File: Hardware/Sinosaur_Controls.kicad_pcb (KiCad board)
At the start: 2 copper layers, 70.8 x 110 mm, 30 parts, among them J1 Conn_01x12_Pin, J10 Audio_Out_L, J11 Audio_Out_R, J12 USB_C_Receptacle, J14 Conn_01x01_Socket, J2 Conn_01x12_Pin, J3 Conn_01x10_Pin, J4 Conn_01x10_Pin, J5 WavetablePosA, J6 WavetablePosB, J7 WarpCV, J8 VOct, J9 VCA, SW1 B_Octave, SW2 Mode_Switch, SW3 Octave_Switch, SW4 ChB_Output, SW5 Encoder, U1 STF202-22T1G

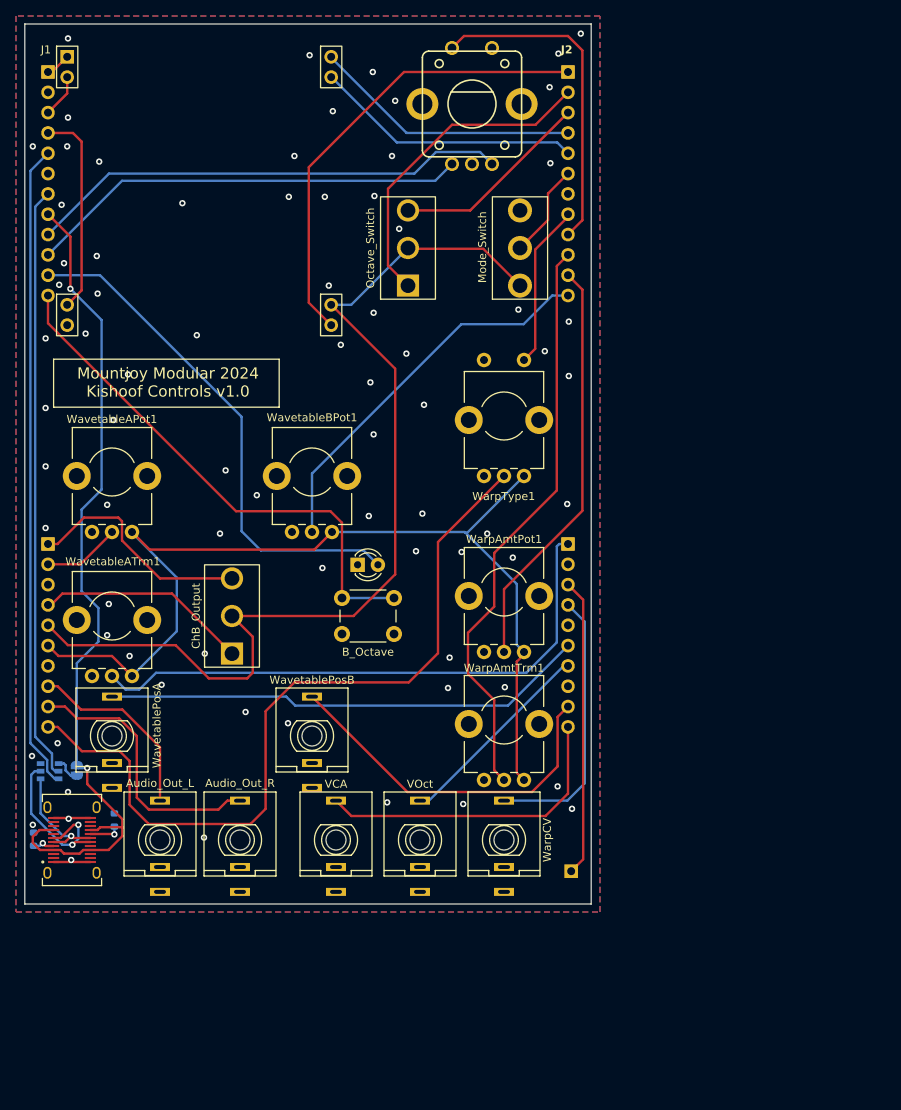
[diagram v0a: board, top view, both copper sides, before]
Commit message: Started control layout
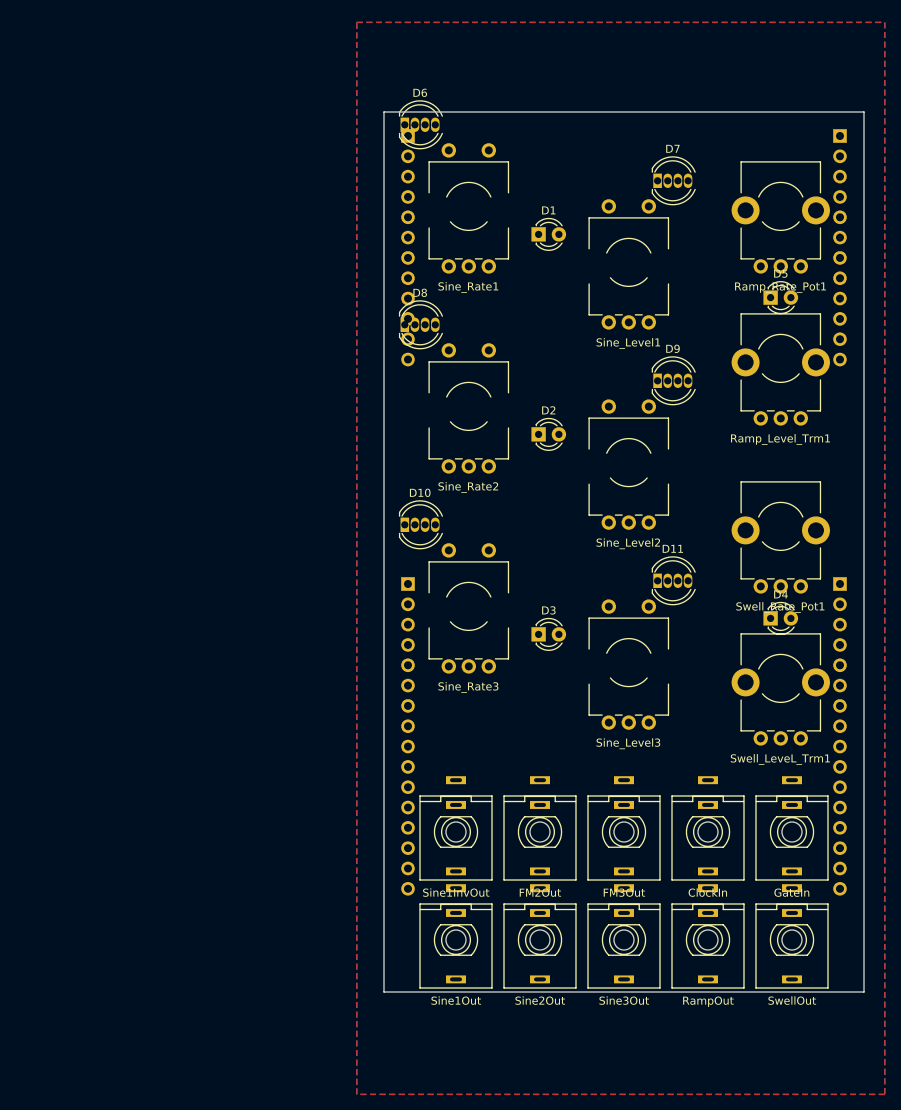
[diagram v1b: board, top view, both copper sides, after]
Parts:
- removed JP1: Jumper, Jumper:SolderJumper-2_P1.3mm_Open_RoundedPad1.0x1.5mm
- removed R1, R2: 5k1, Resistor_SMD:R_0603_1608Metric
- removed SW1: B_Octave, Custom_Footprints:SW_PUSH_6mm_aligned
- removed SW2: Mode_Switch, Custom_Footprints:SPDT_Miniature
- removed SW3: Octave_Switch, Custom_Footprints:SP3T_Mini_Switch
- removed SW4: ChB_Output, Custom_Footprints:SP3T_Mini_Switch
- removed SW5: Encoder, Custom_Footprints:Encoder
- removed U1: STF202-22T1G, Custom_Footprints:STF202-22T1G
- removed U2: ~, Custom_Footprints:LCD_Riser
- removed WarpAmtPot1, WarpAmtTrm1, WavetableAPot1, WavetableATrm1, WavetableBPot1: B10k, Custom_Footprints:Alpha_9mm_Potentiometer_Aligned
- removed WarpType1: WarpTypePot, Custom_Footprints:Bourns_Switch_Potentiometer
- added D10: LED_BGAR, LED_THT:LED_D5.0mm-4_RGB, F.Cu at (102.6, 101.6)
- added D11: LED_BGAR, LED_THT:LED_D5.0mm-4_RGB, F.Cu at (134.2, 108.6)
- added D2: LED, LED_THT:LED_D3.0mm_FlatTop, F.Cu at (119.3, 90.3)
- added D3: LED, LED_THT:LED_D3.0mm_FlatTop, F.Cu at (119.3, 115.3)
- added D4: LED, LED_THT:LED_D3.0mm_FlatTop, F.Cu at (148.3, 113.3)
- added D5: LED, LED_THT:LED_D3.0mm_FlatTop, F.Cu at (148.3, 73.2)
- added D6: LED_BGAR, LED_THT:LED_D5.0mm-4_RGB, F.Cu at (102.6, 51.6)
- added D7: LED_BGAR, LED_THT:LED_D5.0mm-4_RGB, F.Cu at (134.2, 58.6)
- added D8: LED_BGAR, LED_THT:LED_D5.0mm-4_RGB, F.Cu at (102.6, 76.6)
- added D9: LED_BGAR, LED_THT:LED_D5.0mm-4_RGB, F.Cu at (134.2, 83.6)
- added J13: SwellOut, Custom_Footprints:THONKICONN_hole, F.Cu at (151.0, 153.5)
- added Ramp_Level_Trm1: B10k, Custom_Footprints:Alpha_9mm_Potentiometer_Aligned, F.Cu at (149.6, 80.8)
- added Ramp_Rate_Pot1: B10k, Custom_Footprints:Alpha_9mm_Potentiometer_Aligned, F.Cu at (149.6, 61.8)
- added Sine_Level1: Switch_10kPot, Custom_Footprints:Bourns_Switch_Potentiometer, F.Cu at (130.6, 68.8)
- added Sine_Level2: Switch_10kPot, Custom_Footprints:Bourns_Switch_Potentiometer, F.Cu at (130.6, 93.8)
- added Sine_Level3: Switch_10kPot, Custom_Footprints:Bourns_Switch_Potentiometer, F.Cu at (130.6, 118.8)
- added Sine_Rate1: Switch_10kPot, Custom_Footprints:Bourns_Switch_Potentiometer, F.Cu at (110.6, 61.8)
- added Sine_Rate2: Switch_10kPot, Custom_Footprints:Bourns_Switch_Potentiometer, F.Cu at (110.6, 86.8)
- added Sine_Rate3: Switch_10kPot, Custom_Footprints:Bourns_Switch_Potentiometer, F.Cu at (110.6, 111.8)
- added Swell_LeveL_Trm1: B10k, Custom_Footprints:Alpha_9mm_Potentiometer_Aligned, F.Cu at (149.6, 120.8)
- added Swell_Rate_Pot1: B10k, Custom_Footprints:Alpha_9mm_Potentiometer_Aligned, F.Cu at (149.6, 101.8)
- D1: value LED_Small -> LED
- J1: value Conn_01x12_Pin -> Conn_01x12_Male
- J10: value Audio_Out_L -> Sine1InvOut
- J11: value Audio_Out_R -> FM2Out
- J12: value USB_C_Receptacle -> FM3Out; footprint Custom_Footprints:USB_C_Receptacle_Amphenol_12401951E412A -> Custom_Footprints:THONKICONN_hole
- J14: value Conn_01x01_Socket -> ClockIn; footprint Connector_PinHeader_2.54mm:PinHeader_1x01_P2.54mm_Vertical -> Custom_Footprints:THONKICONN_hole; moved to F.Cu
- J2: value Conn_01x12_Pin -> Conn_01x16_Male; footprint Connector_PinSocket_2.54mm:PinSocket_1x12_P2.54mm_Vertical -> Connector_PinSocket_2.54mm:PinSocket_1x16_P2.54mm_Vertical
- J3: value Conn_01x10_Pin -> Conn_01x12_Male; footprint Connector_PinSocket_2.54mm:PinSocket_1x10_P2.54mm_Vertical -> Connector_PinSocket_2.54mm:PinSocket_1x12_P2.54mm_Vertical
- J4: value Conn_01x10_Pin -> Conn_01x16_Male; footprint Connector_PinSocket_2.54mm:PinSocket_1x10_P2.54mm_Vertical -> Connector_PinSocket_2.54mm:PinSocket_1x16_P2.54mm_Vertical
- J5: value WavetablePosA -> Sine1Out
- J6: value WavetablePosB -> Sine2Out
- J7: value WarpCV -> Sine3Out
- J8: value VOct -> RampOut
- J9: value VCA -> GateIn
- moved J1 99.3 mm to (157.0, 53.0)
- moved J2 72.5 mm to (157.0, 109.0)
- moved J12 69.0 mm to (130.0, 140.0), turned to 180 degrees
- moved J3 68.0 mm to (103.0, 53.0)
- moved J9 57.0 mm to (151.0, 140.0), turned to 180 degrees
- moved J5 50.0 mm to (109.0, 153.5), turned to 180 degrees
- moved D1 47.1 mm to (119.3, 65.3)
- moved J6 38.2 mm to (119.5, 153.5), turned to 180 degrees
- moved J8 38.1 mm to (140.5, 153.5), turned to 180 degrees
- moved J11 37.5 mm to (119.5, 140.0), turned to 180 degrees
- moved J10 37.0 mm to (109.0, 140.0), turned to 180 degrees
- moved J4 20.6 mm to (103.0, 109.0)
- moved J7 19.5 mm to (130.0, 153.5), turned to 180 degrees
- moved J14 17.8 mm to (140.5, 140.0)
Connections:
- net /Audio_Out_L renamed /Sine1_Inv_Out
- D1 pad 2: /LED_Oct_B_Out -> /Sine1_LED
- J1 pad 1: /LCD_SPI3_MOSI -> GND
- J1 pad 10: /Encoder_Up -> GND
- J1 pad 11: /LED_Oct_B_Out -> /Ramp_Level
- J1 pad 12: /B_Octave_Btn -> /Sine2_Swell_Rate_LED
- J1 pad 2: GND -> /FM3_Out
- J1 pad 3: /LCD_SPI3_SCK -> /FM2_Out
- J1 pad 4: /LCD_SPI3_SS -> /Ramp_Out
- J1 pad 5: /USB_DP -> /Swell_Out
- J1 pad 6: GND -> /Sine1_Level
- J1 pad 7: /USB_DM -> /Sine2_Level
- J1 pad 8: /USB_VBUS -> /Sine3_Rate
- J1 pad 9: /Encoder_Down -> /Ramp_Rate
- J11 pad 3: /Audio_Out_R -> /FM2_Out
- J14 pad 1: /Ext_Audio_In -> GND
- J2 pad 1: /LCD_Backlight -> /Sine1_Swell_Rate_LED
- J2 pad 10: /Warp_Amt_Trm -> /Sine3_Swell_Lvl_LED
- J2 pad 11: /Warp_Amt_Pot -> /Sine1_Ramp_Rate_LED
- J2 pad 12: /Wavetable_Pos_B_Pot -> /Sine2_Rate
- J2 pad 2: /Octave_Up -> /Swell_Rate
- J2 pad 3: /Octave_Down -> /Sine3_Ramp_Rate_LED
- J2 pad 4: /LCD_DC -> /Sine1_Ramp_Lvl_LED
- J2 pad 5: /LCD_RESET -> /Sine2_Ramp_Lvl_LED
- J2 pad 6: /Mode -> GND
- J2 pad 7: GND -> /Sine3_Ramp_Lvl_LED
- J2 pad 8: /Warp_Polarity_Btn -> /Sine1_Swell_Lvl_LED
- J2 pad 9: /Encoder_Btn -> /Sine2_Swell_Lvl_LED
- J3 pad 1: /ChB_RM -> /Gate_Normal
- J3 pad 10: /Warp_Type_Pot -> GND
- J3 pad 2: /Wavetable_Pos_A_Pot -> GND
- J3 pad 4: /ChB_Mix -> /Sine2_Out
- J3 pad 5: +3.3V -> /Sine3_Out
- J3 pad 6: +3.3VA -> /Sine3_Level
- J3 pad 7: GND -> /Sine1_Out
- J3 pad 9: /Audio_Out_R -> +3.3VA
- J4 pad 1: /Wavetable_Pos_A_Trm -> /Sine3_Swell_Rate_LED
- J4 pad 10: /VCA_CV_In -> /Sine2_Rate_Btn
- J4 pad 2: GND -> /Sine2_LED
- J4 pad 3: /Ext_Audio_In -> /Sine1_LED
- J4 pad 4: /Warp_CV_In -> /Swell_LED
- J4 pad 5: GND -> /Ramp_LED
- J4 pad 6: /Wavetable_Pos_A_CV_In -> /Sine2_Ramp_Rate_LED
- J4 pad 7: /Pitch_CV_In -> /Sine3_LED
- J4 pad 9: /Wavetable_Pos_B_CV_In -> /Sine3_Rate_Btn
- J5 pad 2: GND -> unconnected-(J5-Pad2)
- J5 pad 3: /Wavetable_Pos_A_CV_In -> /Sine1_Out
- J6 pad 2: GND -> unconnected-(J6-Pad2)
- J6 pad 3: /Wavetable_Pos_B_CV_In -> /Sine2_Out
- J7 pad 2: GND -> unconnected-(J7-Pad2)
- J7 pad 3: /Warp_CV_In -> /Sine3_Out
- J8 pad 2: GND -> unconnected-(J8-Pad2)
- J8 pad 3: /Pitch_CV_In -> /Ramp_Out
- J9 pad 2: GND -> /Gate_Normal
- J9 pad 3: /VCA_CV_In -> /Gate_In
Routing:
- net +3.3V: track 124.9 -> 0.00 mm
- net +3.3VA: track 123.5 -> 0.00 mm
- net /USB_VBUS: track 107.0 -> 0.00 mm, vias 2 -> 0
- net /Warp_Type_Pot: track 98.5 -> 0.00 mm
- net /USB_DP: track 80.8 -> 0.00 mm
- net /USB_DM: track 74.3 -> 0.00 mm
- net /Warp_Amt_Trm: track 72.7 -> 0.00 mm
- net /Wavetable_Pos_A_Trm: track 72.3 -> 0.00 mm
- net /B_Octave_Btn: track 66.4 -> 0.00 mm
- net /LED_Oct_B_Out: track 64.6 -> 0.00 mm
- net /Wavetable_Pos_A_CV_In: track 60.6 -> 0.00 mm
- net /Encoder_Down: track 60.4 -> 0.00 mm
- net /LCD_Backlight: track 58.2 -> 0.00 mm
- net /Encoder_Up: track 55.2 -> 0.00 mm
- net /Warp_Amt_Pot: track 51.9 -> 0.00 mm
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- added copper zone on B.Cu, net (none)
- added copper zone on F.Cu, net (none)
- removed copper zone on B.Cu, net GND
- removed copper zone on F.Cu, net GND
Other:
- board size 70.8 x 110 mm -> 60 x 110 mm
- board text removed: "Ext"
- board text removed: "J1"
- board text removed: "J2"
- board text removed: "Mountjoy Modular 2024 Kishoof Controls v1.0"

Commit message: Control PCB wiring
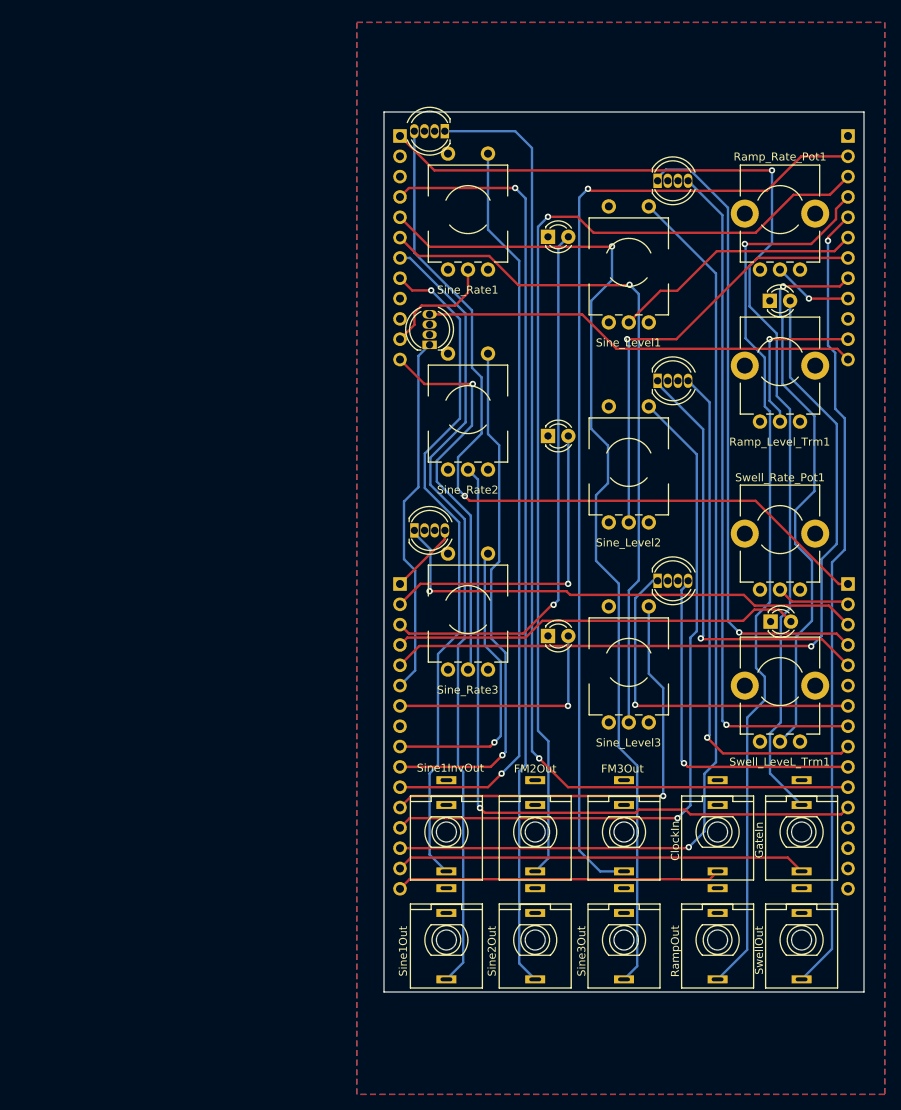
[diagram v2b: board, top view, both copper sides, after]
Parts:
- moved D6 5.06 mm to (107.6, 52.4), turned to 180 degrees
- moved D8 3.98 mm to (105.7, 79.1), turned to 90 degrees
- moved D10 1.39 mm to (103.8, 102.3)
- moved D1 1.21 mm to (120.5, 65.6)
- moved J10 1.20 mm to (107.8, 140.0)
- moved J5 1.20 mm to (107.8, 153.5)
- moved J13 1.20 mm to (152.2, 153.5)
- moved J14 1.20 mm to (141.7, 140.0)
- moved J8 1.20 mm to (141.7, 153.5)
- moved J9 1.20 mm to (152.2, 140.0)
- moved D2 1.19 mm to (120.5, 90.5)
- moved D3 1.19 mm to (120.5, 115.5)
- moved J1 1.00 mm to (158.0, 53.0)
- moved J2 1.00 mm to (102.0, 53.0)
- moved J3 1.00 mm to (158.0, 109.0)
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- renumbered J3 to J2, J2 to J3
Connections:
- J1 pad 8: /Sine3_Rate -> /Swell_Level
- J2 pad 12: /Swell_Level -> /Sine3_Rate
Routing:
- net /Gate_Normal: track 0.00 -> 133.6 mm, vias 0 -> 1
- net /Sine1_Ramp_Rate_LED: track 0.00 -> 128.5 mm, vias 0 -> 1
- net /Sine3_Out: track 0.00 -> 125.1 mm, vias 0 -> 1
- net /FM2_Out: track 0.00 -> 124.8 mm, vias 0 -> 1
- net /FM3_Out: track 0.00 -> 124.2 mm, vias 0 -> 1
- net /Sine1_Lvl_Btn: track 0.00 -> 121.1 mm, vias 0 -> 1
- net /Sine2_Out: track 0.00 -> 115.5 mm, vias 0 -> 1
- net /Ramp_Out: track 0.00 -> 112.9 mm, vias 0 -> 1
- net /Sine1_Swell_Rate_LED: track 0.00 -> 103.1 mm, vias 0 -> 1
- net /Swell_Out: track 0.00 -> 99.4 mm, vias 0 -> 1
- net /Sine1_Out: track 0.00 -> 99.4 mm
- net /Ramp_LED: track 0.00 -> 99.4 mm, vias 0 -> 1
- net /Sine1_Rate_Btn: track 0.00 -> 93.4 mm, vias 0 -> 1
- net /Sine2_Lvl_Btn: track 0.00 -> 90.2 mm, vias 0 -> 1
- net /Sine2_Rate: track 0.00 -> 89.9 mm, vias 0 -> 1
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
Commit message: Updates to LEDs
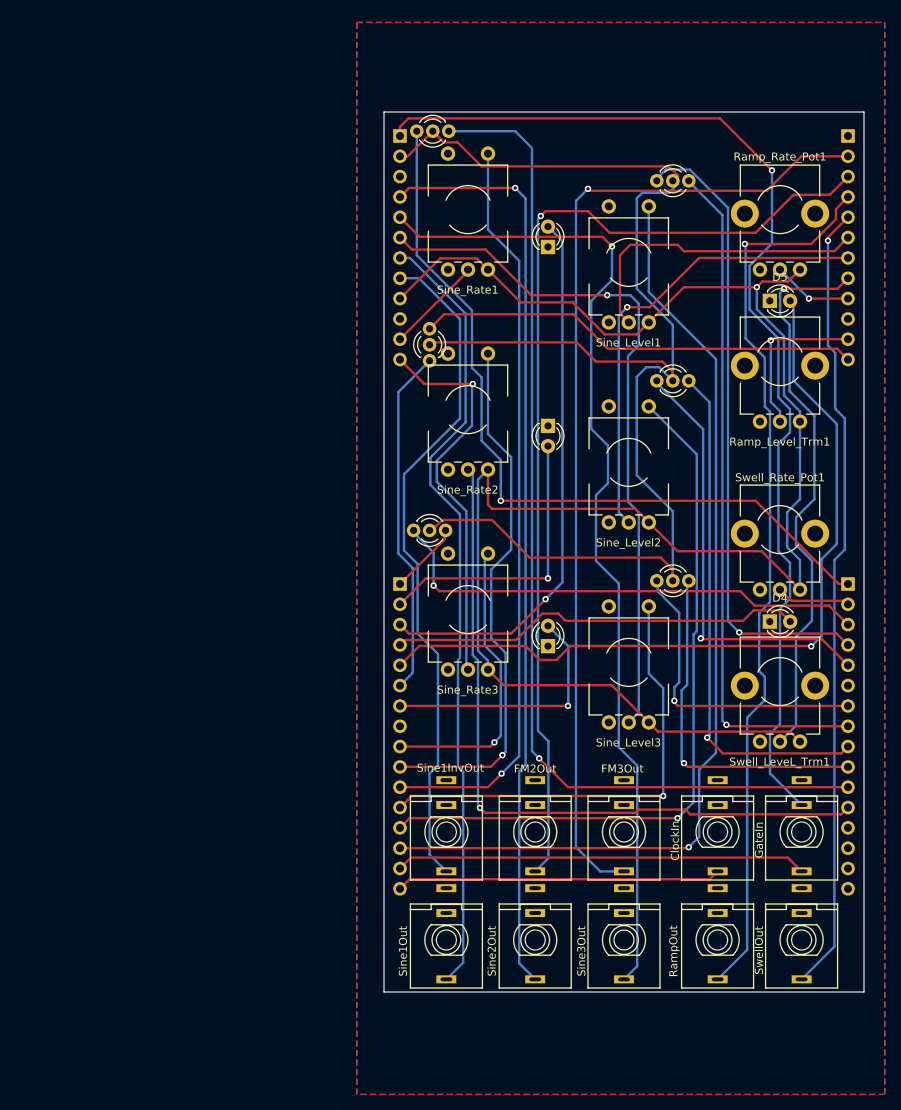
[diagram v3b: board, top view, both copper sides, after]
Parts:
- D1, D2, D3, D4, D5: footprint LED_THT:LED_D3.0mm_FlatTop -> Custom_Footprints:LED_D3.0mm
- D10, D11, D6, D7, D8, D9: value LED_BGAR -> LED_Dual_KAK; footprint LED_THT:LED_D5.0mm-4_RGB -> Custom_Footprints:LED_D3.0mm-3
- moved D10 1.90 mm to (105.7, 102.3)
- moved D11 1.90 mm to (136.1, 108.6)
- moved D7 1.90 mm to (136.1, 58.6)
- moved D9 1.90 mm to (136.1, 83.6)
- moved D6 1.50 mm to (106.1, 52.4)
- moved D5 1.28 mm to (149.5, 73.6)
- moved D4 1.18 mm to (149.5, 113.7)
- turned D1 to 90 degrees
- turned D2 to -90 degrees
- turned D3 to 90 degrees
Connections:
- D10 pad 2: unconnected-(D10-GK-Pad2) -> +3.3V
- D10 pad 3: +3.3V -> /Sine3_Swell_Rate_LED
- D11 pad 2: unconnected-(D11-GK-Pad2) -> +3.3V
- D11 pad 3: +3.3V -> /Sine3_Swell_Lvl_LED
- D6 pad 2: unconnected-(D6-GK-Pad2) -> +3.3V
- D6 pad 3: +3.3V -> /Sine1_Swell_Rate_LED
- D7 pad 2: unconnected-(D7-GK-Pad2) -> +3.3V
- D7 pad 3: +3.3V -> /Sine1_Swell_Lvl_LED
- D8 pad 2: unconnected-(D8-GK-Pad2) -> +3.3V
- D8 pad 3: +3.3V -> /Sine2_Swell_Rate_LED
- D9 pad 2: unconnected-(D9-GK-Pad2) -> +3.3V
- D9 pad 3: +3.3V -> /Sine2_Swell_Lvl_LED
- J2 pad 2: GND -> +3.3V
- J3 pad 14: +3.3V -> GND
- J3 pad 16: unconnected-(J3-Pin_16-Pad16) -> GND
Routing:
- net +3.3VA: track 0.00 -> 217.3 mm, vias 0 -> 1
- net +3.3V: track 0.00 -> 170.6 mm
- net /Sine1_Level: track 31.8 -> 38.9 mm
- net /Sine3_Ramp_Lvl_LED: track 43.7 -> 38.5 mm
- net /Sine1_Swell_Rate_LED: track 103.1 -> 98.3 mm
- net /Sine2_LED: track 40.6 -> 36.4 mm
- net /Gate_Normal: track 133.6 -> 137.2 mm
- net /Sine2_Level: track 54.8 -> 58.0 mm
- net /Sine1_Rate: track 14.7 -> 12.2 mm
- net /Sine3_LED: track 29.8 -> 32.1 mm
- net /Sine2_Ramp_Rate_LED: track 45.3 -> 43.6 mm
- net /Ramp_LED: track 99.4 -> 100.8 mm
- net /Sine2_Rate_Btn: track 65.5 -> 66.8 mm
- net /FM2_Out: track 124.8 -> 126.0 mm
- net /Sine3_Ramp_Rate_LED: track 62.5 -> 61.7 mm
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- added copper zone on B.Cu, net GND
- added copper zone on F.Cu, net GND
- removed copper zone on B.Cu, net (none)
- removed copper zone on F.Cu, net (none)

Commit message: Gerber production
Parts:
- moved D8 1.90 mm to (105.7, 77.2)
- turned D10 to 180 degrees
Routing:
- net /Sine1_Rate_Btn: track 93.4 -> 97.7 mm
- net /Sine2_Ramp_Rate_LED: track 43.6 -> 47.9 mm
- net /Sine2_Out: track 115.5 -> 119.1 mm
- net /Sine3_Ramp_Rate_LED: track 61.7 -> 59.9 mm
- net /Sine3_LED: track 32.1 -> 30.3 mm
- net /Sine3_Swell_Rate_LED: track 9.02 -> 7.40 mm
- net +3.3V: track 170.6 -> 169.3 mm
- net /Sine1_Rate: track 12.2 -> 13.4 mm
- net /FM3_Out: track 124.6 -> 123.4 mm
- net /Ramp_LED: track 100.8 -> 99.7 mm
- net /Sine1_LED: track 68.6 -> 69.6 mm
- net /Sine3_Ramp_Lvl_LED: track 38.5 -> 37.6 mm
- net /Swell_Out: track 99.4 -> 98.7 mm, vias 1 -> 0
- net /Swell_LED: track 51.9 -> 51.1 mm
- net /Sine2_Swell_Rate_LED: track 55.4 -> 54.7 mm
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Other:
- board text added: "J1"
- board text added: "J2"
- board text added: "J3"
- board text added: "J4"
- board text added: "Mountjoy Modular 2024 Sinosaur Controls v1.0"

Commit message: Gerber production for v1
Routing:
- net GND: vias 1 -> 24
